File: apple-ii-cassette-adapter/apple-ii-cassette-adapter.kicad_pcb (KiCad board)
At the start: 2 copper layers, 21 parts, among them J1 LCD_I2C, J2 POWER, J3 ADAFRUIT_SDCARD, J4 AUDIO, J5 AUDIO, J6 BUTTONS, SW1 PLAY, SW2 STOP, SW3 PREV, SW4 NEXT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

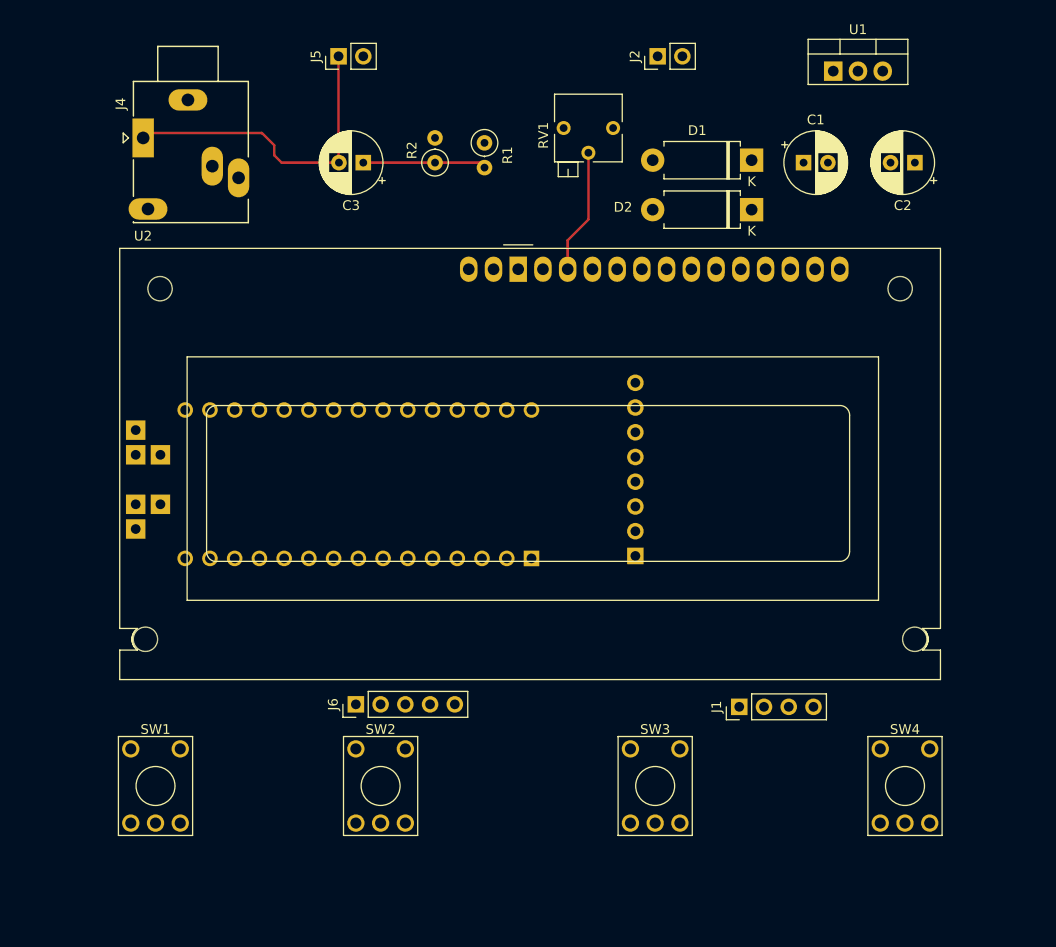
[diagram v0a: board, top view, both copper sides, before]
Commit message: In progress schematic layout
For some reason I don't have a ground pin on this audio jack footprint; i need
to figure THAT out soon.
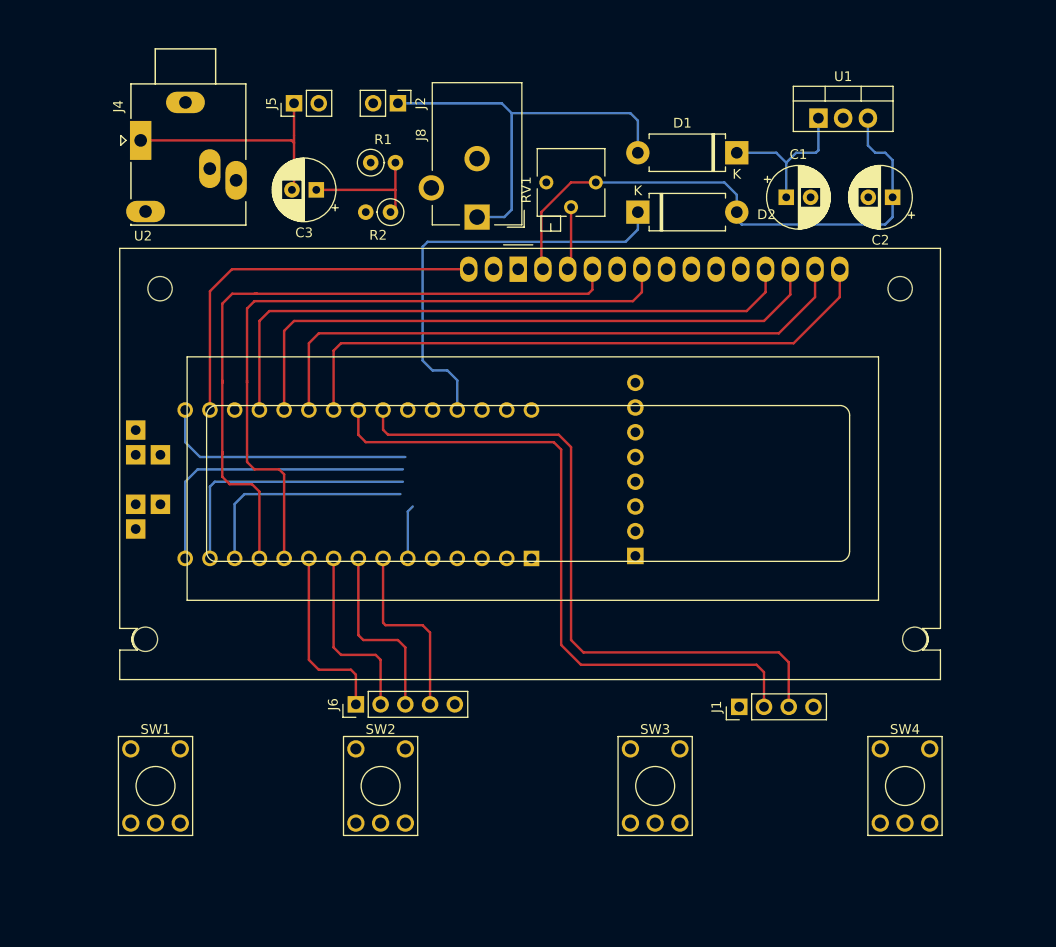
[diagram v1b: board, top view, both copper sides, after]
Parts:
- added J8: DC Input, Connector_BarrelJack:BarrelJack_CUI_PJ-102AH_Horizontal, F.Cu at (59.2, 39.6)
- moved J2 27.1 mm to (51.1, 27.9), turned to 270 degrees
- moved R1 11.9 mm to (48.3, 34.0), turned to 0 degrees
- moved D2 11.7 mm to (75.7, 39.1), turned to 0 degrees
- moved R2 6.83 mm to (50.3, 39.1), turned to 180 degrees
- moved J5 6.65 mm to (40.4, 27.9)
- moved RV1 5.86 mm to (66.3, 36.1)
- moved C3 5.58 mm to (42.7, 36.8)
- moved U1 5.06 mm to (94.2, 29.5)
- moved C2 4.23 mm to (101.9, 37.6)
- moved C1 3.98 mm to (90.9, 37.6)
- moved D1 1.70 mm to (85.9, 33.0)
- moved J4 0.36 mm to (24.6, 31.8)
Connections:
- net Net-(D1-Pad2) renamed PWR_IN
- U2 pad 4: LCD_D8 -> LCD_D9
- U2 pad 6: LCD_D9 -> LCD_D8
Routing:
- net LCD_D8: track 0.00 -> 72.6 mm
- net LCD_D9: track 0.00 -> 70.5 mm
- net LCD_I2C_SCL: track 0.00 -> 69.8 mm
- net LCD_I2C_SDA: track 0.00 -> 69.6 mm
- net LCD_A0: track 0.00 -> 65.0 mm
- net LCD_A1: track 0.00 -> 64.3 mm
- net LCD_A2: track 0.00 -> 63.7 mm
- net LCD_A3: track 0.00 -> 63.2 mm
- net +5V: track 0.00 -> 58.7 mm
- net Net-(A1-Pad27): track 0.00 -> 43.7 mm
- net PWR_IN: track 0.00 -> 42.5 mm
- net +3V3: track 0.00 -> 39.7 mm
- net SDCARD_DO: track 0.00 -> 30.8 mm
- net SDCARD_DI: track 0.00 -> 27.4 mm
- net SDCARD_CLK: track 0.00 -> 26.5 mm
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
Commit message: Update schematic/PCB; this may actually work.
"S" is the shield; not GND. Weird. Anyway, that's GND now.
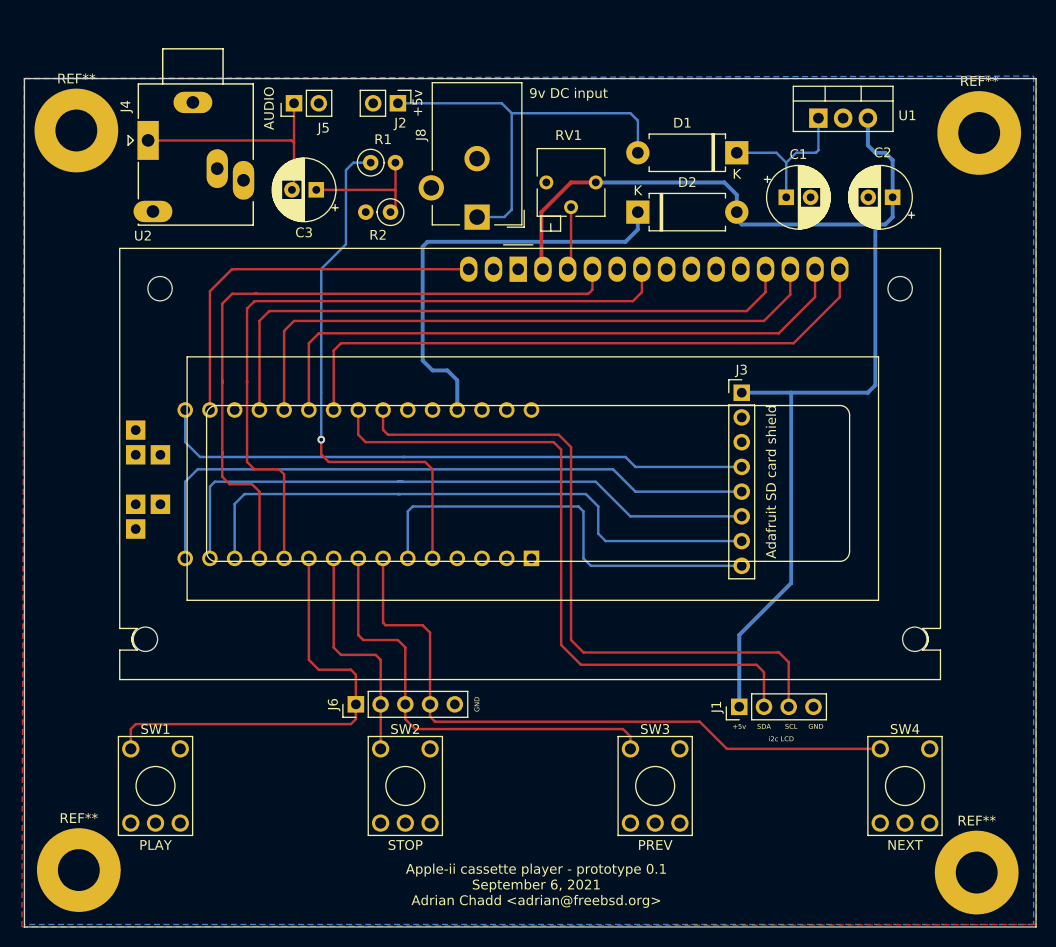
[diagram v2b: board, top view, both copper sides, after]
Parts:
- added REF**: MountingHole_4.3mm_M4_Pad, MountingHole:MountingHole_4.3mm_M4_Pad, F.Cu at (110.5, 106.9)
- added REF**: MountingHole_4.3mm_M4_Pad, MountingHole:MountingHole_4.3mm_M4_Pad, F.Cu at (18.3, 106.7)
- added REF**: MountingHole_4.3mm_M4_Pad, MountingHole:MountingHole_4.3mm_M4_Pad, F.Cu at (18.0, 30.7)
- added REF**: MountingHole_4.3mm_M4_Pad, MountingHole:MountingHole_4.3mm_M4_Pad, F.Cu at (110.7, 31.0)
- J3: moved to F.Cu
- moved J3 20.0 mm to (86.4, 57.7)
- moved SW2 2.54 mm to (49.3, 94.2)
- moved J4 0.76 mm to (25.4, 31.8)
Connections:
- J4 pad R: (no net) -> Net-(J4-PadR)
- J4 pad RN: (no net) -> Net-(J4-PadRN)
- J4 pad S: Net-(J4-PadS) -> GND
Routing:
- net +5V: track 58.7 -> 123.7 mm
- net NANO_AUDIO_OUTPUT: track 0.00 -> 54.3 mm, vias 0 -> 1
- net BUTTON_NEXT: track 19.2 -> 68.1 mm
- net SDCARD_CD: track 5.54 -> 44.7 mm
- net SDCARD_CS: track 23.0 -> 62.0 mm
- net SDCARD_DI: track 27.4 -> 64.2 mm
- net SDCARD_DO: track 30.8 -> 66.5 mm
- net SDCARD_CLK: track 26.5 -> 61.8 mm
- net BUTTON_PLAY: track 18.9 -> 46.0 mm
- net BUTTON_PREV: track 19.1 -> 45.7 mm
- net BUTTON_STOP: track 19.1 -> 23.6 mm
- added copper zone on B.Cu, net GND
- added copper zone on F.Cu, net GND
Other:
- board outline added: 103.9 x 87.1 mm
- board text added: "+5v"
- board text added: "9v DC input"
- board text added: "AUDIO"
- board text added: "Adafruit SD card shield"
- board text added: "Apple-ii cassette player - prototype 0.1 September 6, 2021 Adrian Chadd <adrian@freebsd.org>"
- board text added: "GND"
- board text added: "NEXT"
- board text added: "PLAY"
- board text added: "PREV"
- board text added: "SCL"
- board text added: "SDA"
- board text added: "STOP"
- board text added: "i2c LCD"

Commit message: Route the audio path over buttons, /not/ over the SD card IO bus.
This also saves a via.
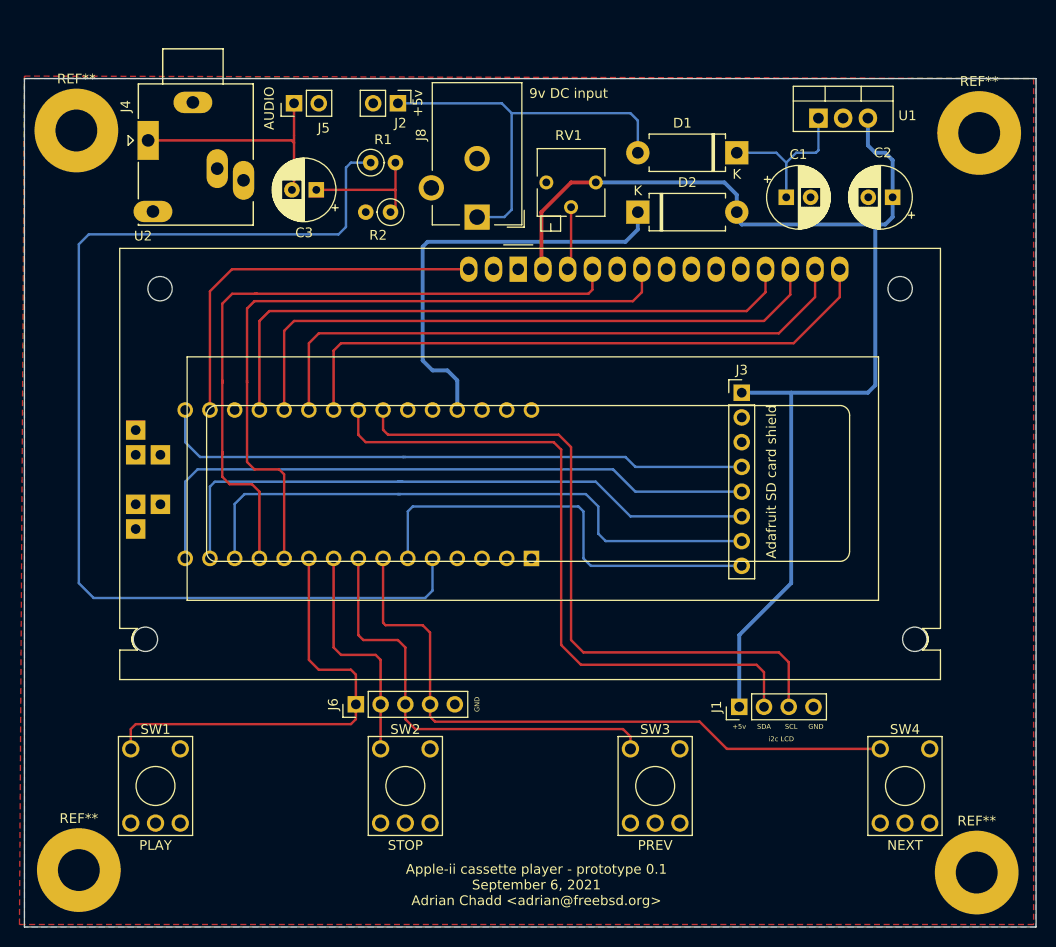
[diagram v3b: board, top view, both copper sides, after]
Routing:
- net NANO_AUDIO_OUTPUT: track 54.3 -> 112.4 mm, vias 1 -> 0
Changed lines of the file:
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@@
     (thickness 1.6)
     (drawings 22)
-    (tracks 213)
+    (tracks 211)
     (zones 0)
     (modules 26)
@@
   (segment (start 88.646 50.292) (end 40.386 50.292) (width 0.25) (layer F.Cu) (net 6))
   (segment (start 91.347001 44.978001) (end 91.347001 47.590999) (width 0.25) (layer F.Cu) (net 6))
-  (segment (start 48.26 34.036) (end 46.482 34.036) (width 0.25) (layer B.Cu) (net 7))
-  (segment (start 46.482 34.036) (end 45.72 34.798) (width 0.25) (layer B.Cu) (net 7))
-  (segment (start 45.72 34.798) (end 45.72 42.418) (width 0.25) (layer B.Cu) (net 7))
-  (segment (start 45.72 42.418) (end 43.18 44.958) (width 0.25) (layer B.Cu) (net 7))
-  (segment (start 43.18 44.958) (end 43.18 57.658) (width 0.25) (layer B.Cu) (net 7))
-  (segment (start 43.18 57.658) (end 43.18 62.484) (width 0.25) (layer B.Cu) (net 7))
-  (segment (start 43.18 62.484) (end 43.18 62.484) (width 0.25) (layer B.Cu) (net 7))
-  (via (at 43.18 62.484) (size 0.8) (drill 0.4) (layers F.Cu B.Cu) (net 7))
-  (segment (start 54.61 74.676) (end 54.61 65.532) (width 0.25) (layer F.Cu) (net 7))
-  (segment (start 54.61 65.532) (end 53.848 64.77) (width 0.25) (layer F.Cu) (net 7))
-  (segment (start 53.848 64.77) (end 43.942 64.77) (width 0.25) (layer F.Cu) (net 7))
-  (segment (start 43.18 64.008) (end 43.18 62.484) (width 0.25) (layer F.Cu) (net 7))
-  (segment (start 43.942 64.77) (end 43.18 64.008) (width 0.25) (layer F.Cu) (net 7))
+  (segment (start 45.72 34.544) (end 46.228 34.036) (width 0.25) (layer B.Cu) (net 7))
+  (segment (start 45.72 40.64) (end 45.72 34.544) (width 0.25) (layer B.Cu) (net 7))
+  (segment (start 44.958 41.402) (end 45.72 40.64) (width 0.25) (layer B.Cu) (net 7))
+  (segment (start 46.228 34.036) (end 48.26 34.036) (width 0.25) (layer B.Cu) (net 7))
+  (segment (start 18.288 42.418) (end 19.304 41.402) (width 0.25) (layer B.Cu) (net 7))
+  (segment (start 19.812 78.74) (end 18.288 77.216) (width 0.25) (layer B.Cu) (net 7))
+  (segment (start 19.304 41.402) (end 44.958 41.402) (width 0.25) (layer B.Cu) (net 7))
+  (segment (start 53.848 78.74) (end 19.812 78.74) (width 0.25) (layer B.Cu) (net 7))
+  (segment (start 54.61 77.978) (end 53.848 78.74) (width 0.25) (layer B.Cu) (net 7))
+  (segment (start 18.288 77.216) (end 18.288 42.418) (width 0.25) (layer B.Cu) (net 7))
+  (segment (start 54.61 74.676) (end 54.61 77.978) (width 0.25) (layer B.Cu) (net 7))
   (segment (start 41.91 52.578) (end 41.91 59.436) (width 0.25) (layer F.Cu) (net 8))
   (segment (start 42.926 51.562) (end 41.91 52.578) (width 0.25) (layer F.Cu) (net 8))
@@
     (polygon
       (pts
-        (xy 116.586 112.268) (xy 12.446 112.522) (xy 12.7 25.4) (xy 116.586 25.4)
+        (xy 116.332 25.4) (xy 116.332 112.268) (xy 12.192 112.268) (xy 12.7 25.146)
       )
     )
@@
     (polygon
       (pts
-        (xy 116.332 112.268) (xy 12.7 112.268) (xy 12.7 25.4) (xy 116.332 25.146)
+        (xy 116.586 112.522) (xy 12.7 112.522) (xy 12.7 25.4) (xy 116.586 25.4)
       )
     )

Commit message: Update routing and schematic for the RC1602A LCD variant.
It's not the adafruit one, and honestly I'm suprised kicad doesn't come with
the adafruit part footprints, but baby steps.
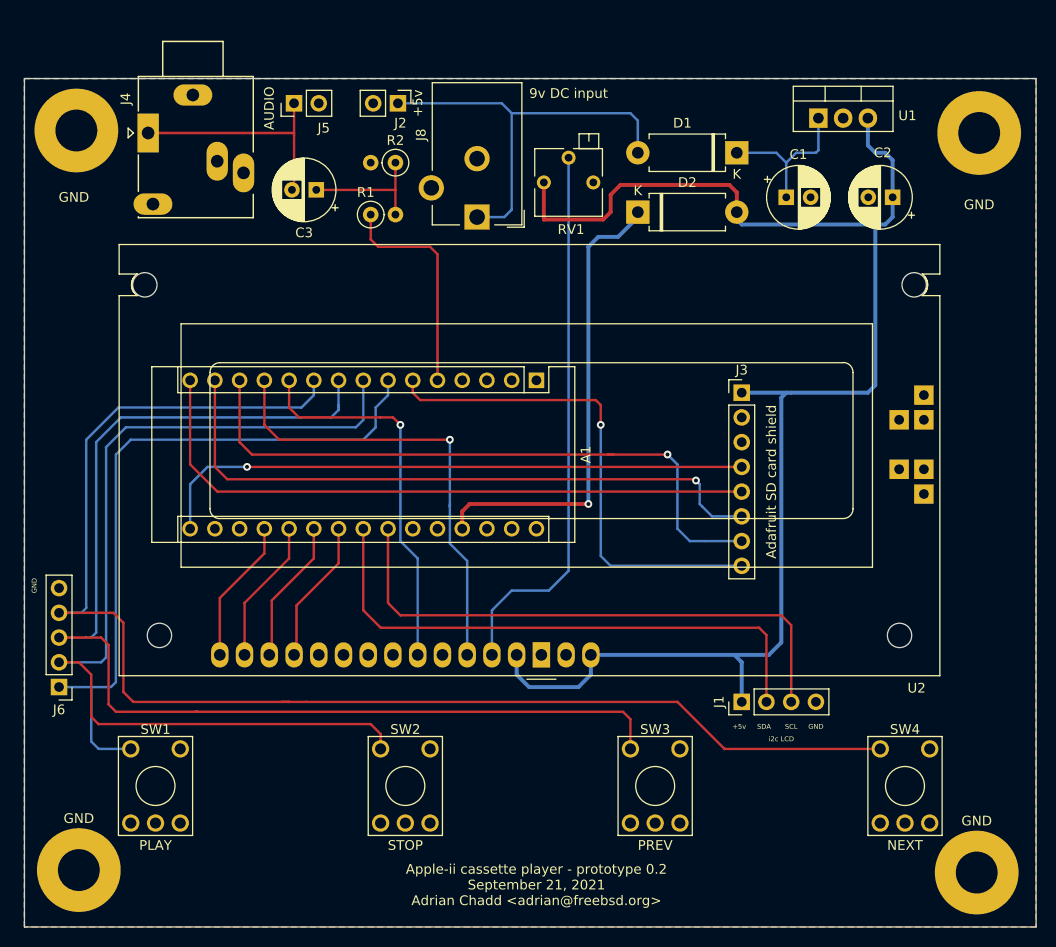
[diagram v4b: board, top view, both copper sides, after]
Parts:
- removed REF** (x3): MountingHole_4.3mm_M4_Pad, MountingHole:MountingHole_4.3mm_M4_Pad
- added GND: MountingHole_4.3mm_M4_Pad, MountingHole:MountingHole_4.3mm_M4_Pad, F.Cu at (110.5, 106.9)
- added GND: MountingHole_4.3mm_M4_Pad, MountingHole:MountingHole_4.3mm_M4_Pad, F.Cu at (18.3, 106.7)
- added GND: MountingHole_4.3mm_M4_Pad, MountingHole:MountingHole_4.3mm_M4_Pad, F.Cu at (110.7, 31.0)
- A1: moved to F.Cu
- U2: value RC1602A -> LCD 16x2
- moved U2 39.7 mm to (65.8, 84.6), turned to 180 degrees
- moved J6 30.5 mm to (16.3, 87.9), turned to 180 degrees
- moved A1 18.3 mm to (65.3, 56.4), turned to 270 degrees
- moved R1 5.33 mm to (48.3, 39.4)
- moved R2 5.11 mm to (50.8, 34.0)
- moved RV1 4.83 mm to (71.1, 36.1), turned to 270 degrees
- moved J4 0.76 mm to (25.4, 31.0)
- moved J1 0.57 mm to (86.4, 89.4)
- renumbered REF** to GND
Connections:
- A1 pad 10: BUTTON_PLAY -> BUTTON_NEXT
- A1 pad 7: BUTTON_NEXT -> BUTTON_PLAY
- A1 pad 8: BUTTON_PREV -> BUTTON_STOP
- A1 pad 9: BUTTON_STOP -> BUTTON_PREV
- U2 pad 11: LCD_A0 -> LCD_A3
- U2 pad 12: LCD_A1 -> LCD_A2
- U2 pad 13: LCD_A2 -> LCD_A1
- U2 pad 14: LCD_A3 -> LCD_A0
- U2 pad 15: +3V3 -> +5V
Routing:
- net NANO_AUDIO_OUTPUT: track 112.4 -> 23.0 mm
- net BUTTON_PREV: track 45.7 -> 122.4 mm
- net BUTTON_STOP: track 23.6 -> 98.4 mm
- net BUTTON_NEXT: track 68.1 -> 142.1 mm
- net LCD_A0: track 65.0 -> 14.8 mm
- net Net-(RV1-Pad2): track 6.51 -> 56.5 mm
- net LCD_A1: track 64.3 -> 14.8 mm
- net LCD_A2: track 63.7 -> 14.8 mm
- net LCD_A3: track 63.2 -> 14.8 mm
- net +3V3: track 39.7 -> 0.00 mm
- net LCD_D8: track 72.6 -> 39.3 mm, vias 0 -> 1
- net +5V: track 123.7 -> 151.9 mm
- net BUTTON_PLAY: track 46.0 -> 72.6 mm
- net LCD_D9: track 70.5 -> 47.3 mm, vias 0 -> 1
- net LCD_I2C_SCL: track 69.8 -> 57.8 mm
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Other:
- board text added: "Apple-ii cassette player - prototype 0.2 September 21, 2021 Adrian Chadd <adrian@freebsd.org>"
- board text removed: "Apple-ii cassette player - prototype 0.1 September 6, 2021 Adrian Chadd <adrian@freebsd.org>"
